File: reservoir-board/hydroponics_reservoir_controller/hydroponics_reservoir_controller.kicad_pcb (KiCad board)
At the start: 2 copper layers, 100 x 100 mm, 82 parts, among them J1 Jumper, J2 Conn_01x04_Socket, J5 i2c_Peripherals, J6 1Wire_Peripherals, Q1 AO3400A, Q2 AO3400A, Q3 AO3400A, Q4 AO3400A, Q5 AO3400A, Q6 AO3400A, Q7 AO3400A, Q8 AO3400A, U1 ESP32, U2 SP3485EN, U3 AMS1117-3.3, U4 TPS54302

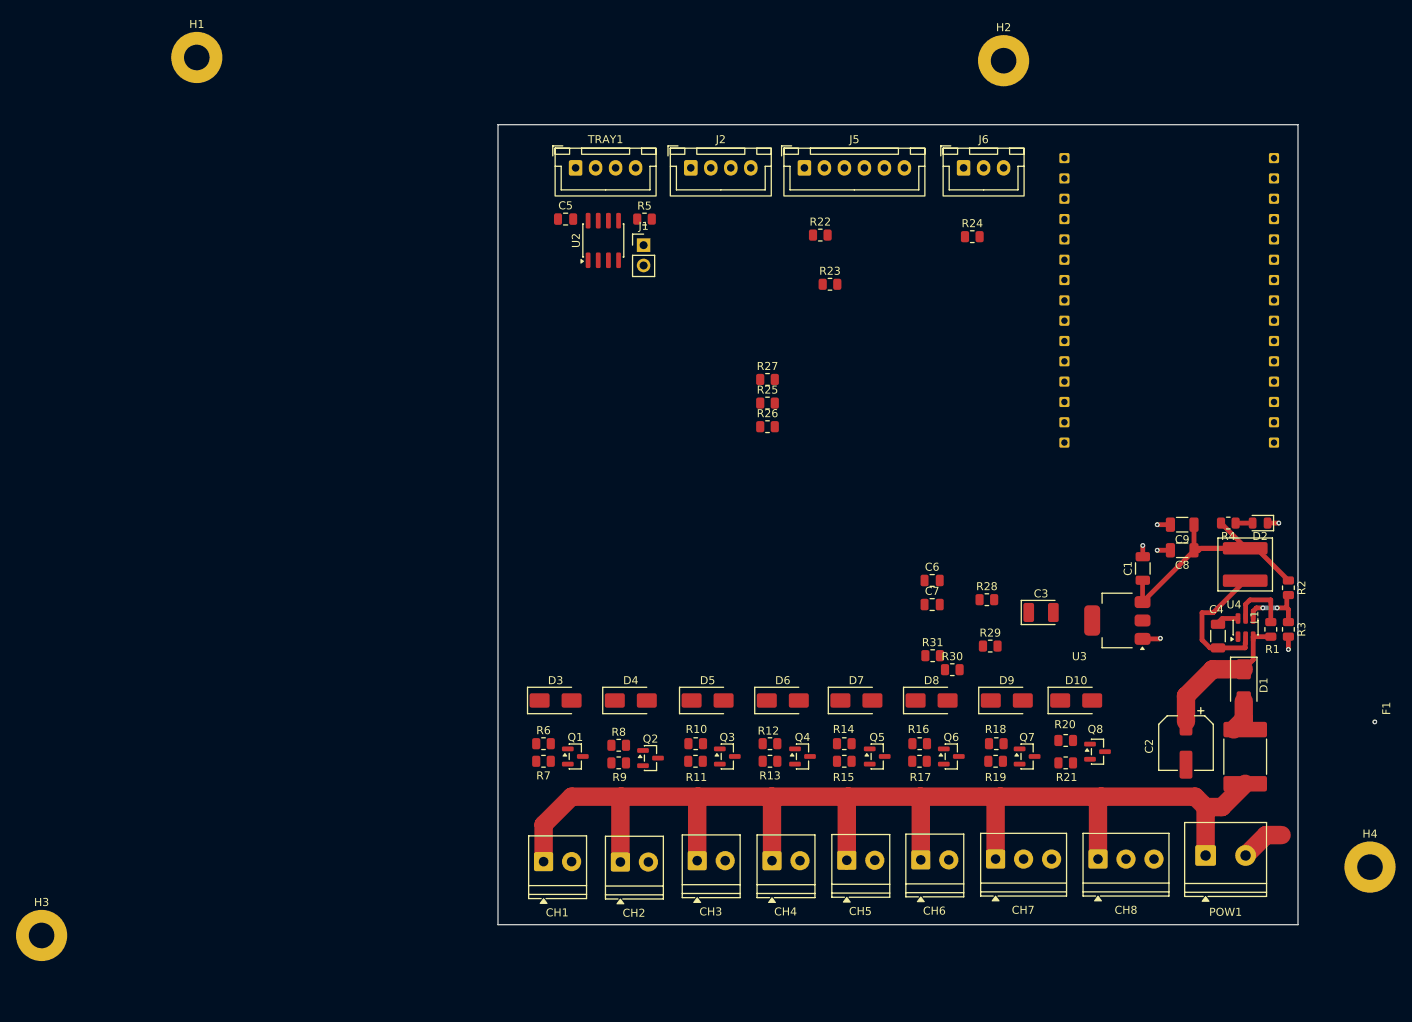
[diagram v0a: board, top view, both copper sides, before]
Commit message: reservoir-board: add PCB routing (traces/vias)
Route the hydroponics_reservoir_controller board layout - adds ~600
track segments and vias. Minor designator-order reshuffle in the
project file.

Co-Authored-By: Claude Sonnet 5 <noreply@anthropic.com>
Claude-Session: https://claude.ai/code/session_01EaqMDfPd3Yu8GaTXYhbk9d
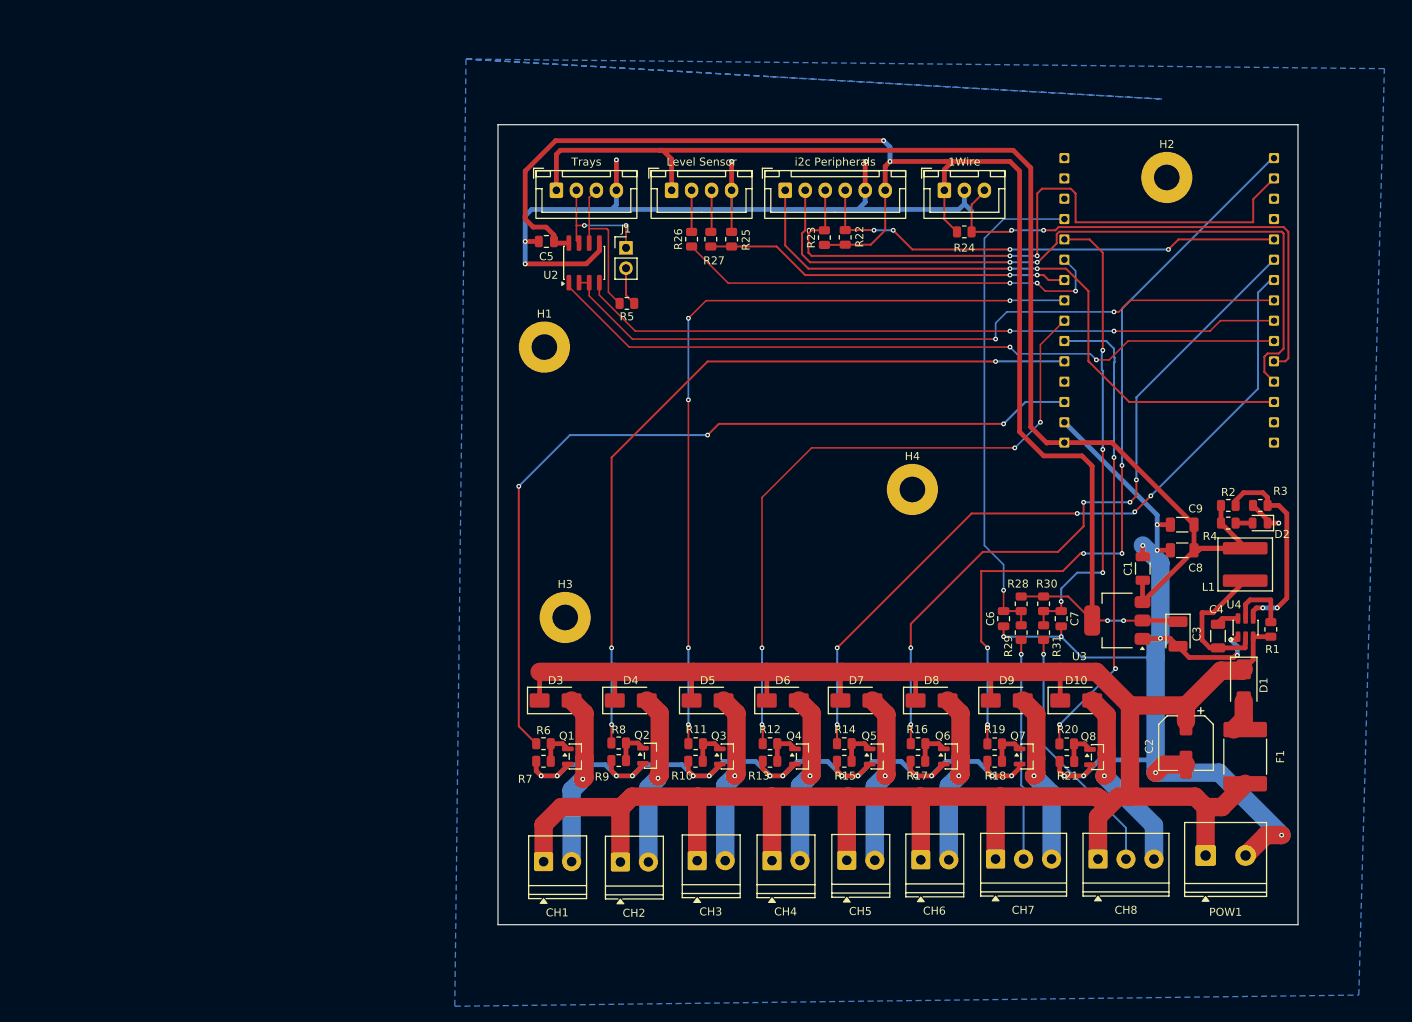
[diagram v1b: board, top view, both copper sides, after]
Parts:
- Level Sensor: renamed from J2
- i2c Peripherals: renamed from J5
- moved H3 76.6 mm to (108.2, 113.0)
- moved H4 74.2 mm to (151.6, 97.0)
- moved H1 56.6 mm to (105.6, 79.2)
- moved R26 25.3 mm to (124.0, 65.7), turned to 90 degrees
- moved H2 25.1 mm to (183.4, 58.0)
- moved R25 21.0 mm to (129.0, 65.7), turned to 90 degrees
- moved R27 18.9 mm to (126.4, 65.7), turned to 90 degrees
- moved C3 17.3 mm to (184.8, 115.1), turned to -90 degrees
- moved C7 16.2 mm to (170.2, 113.2), turned to -90 degrees
- moved R3 15.9 mm to (195.1, 99.0), turned to 180 degrees
- moved R31 14.2 mm to (168.0, 114.9), turned to -90 degrees
- moved R30 14.1 mm to (168.0, 111.3), turned to -90 degrees
- moved R2 12.7 mm to (191.1, 99.0), turned to 0 degrees
- moved R5 10.8 mm to (115.9, 73.7), turned to 180 degrees
- moved C6 10.1 mm to (163.0, 113.2), turned to -90 degrees
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- renumbered J6 to 1Wire, TRAY1 to Trays
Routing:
- net GND: track 15.9 -> 342.3 mm, vias 6 -> 32
- net +3V3: track 0.00 -> 190.6 mm, vias 0 -> 4
- net +5V: track 39.7 -> 164.9 mm
- net +12V: track 176.4 -> 297.0 mm
- net /CH_1_DR: track 0.00 -> 105.6 mm, vias 0 -> 3
- net /CH_3_DR: track 0.00 -> 101.1 mm, vias 0 -> 5
- net /CH_7_DR: track 0.00 -> 97.8 mm, vias 0 -> 5
- net /CH_2_DR: track 0.00 -> 97.3 mm, vias 0 -> 3
- net /ESP32_D5: track 0.00 -> 93.9 mm, vias 0 -> 2
- net /ESP32_RX2: track 0.00 -> 93.4 mm, vias 0 -> 2
- net /CH_5_DR: track 0.00 -> 92.7 mm, vias 0 -> 5
- net /AUX_INT: track 0.00 -> 92.0 mm, vias 0 -> 2
- net /CH_6_DR: track 0.00 -> 88.5 mm, vias 0 -> 5
- net /ESP32_TX2: track 0.00 -> 88.3 mm, vias 0 -> 2
- net /I2C_SCL: track 0.00 -> 83.8 mm, vias 0 -> 2
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- added copper zone on B.Cu, net GND
